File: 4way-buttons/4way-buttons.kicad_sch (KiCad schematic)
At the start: 8 parts, among them J1 Conn_01x08_Male, J2 Conn_01x08_Male, SW1 SW_Push, SW2 SW_Push, SW3 SW_Push, SW4 SW_Push, SW5 SW_Push, SW6 SW_Push

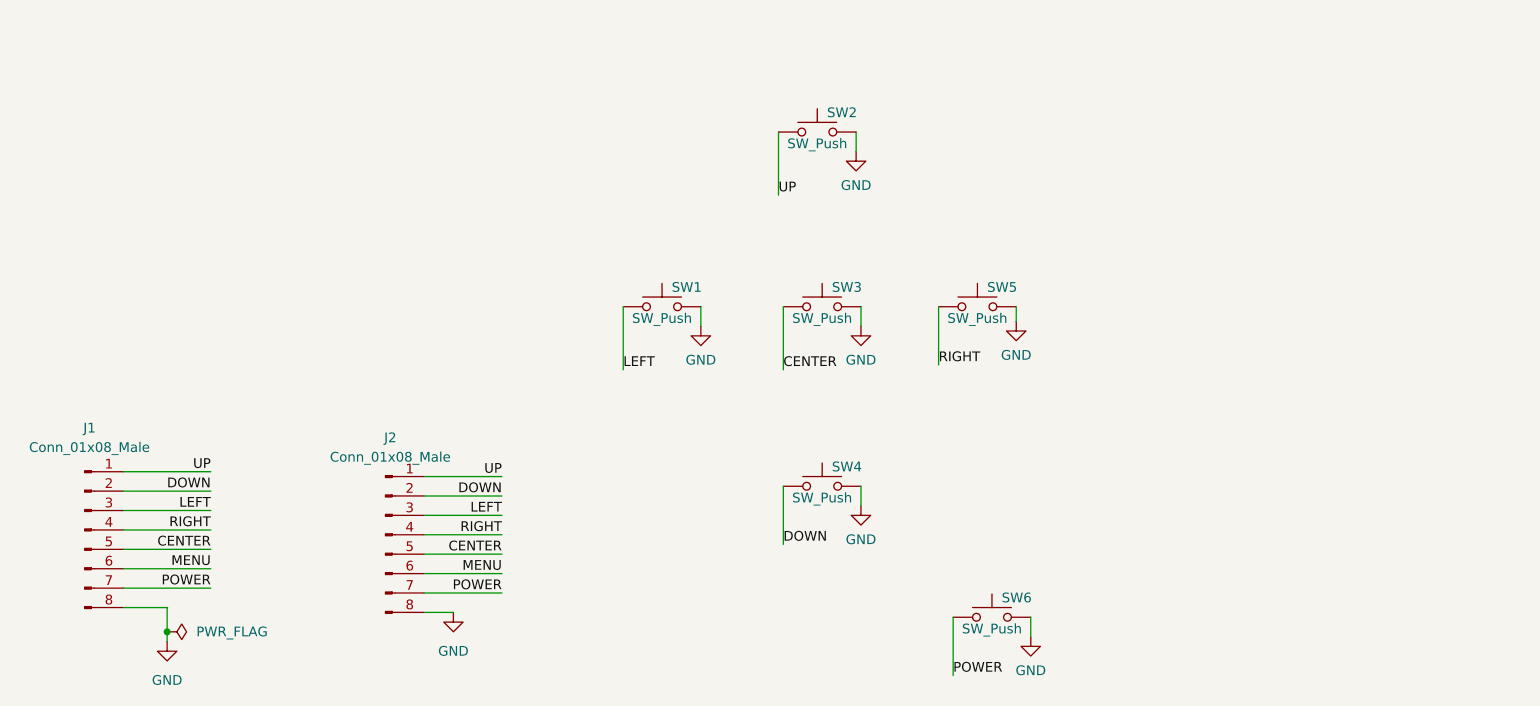
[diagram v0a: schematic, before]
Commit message: 모니터 컨트를 버튼 보드 이미지 추가
Signed-off-by: Ju, Gyeong-min <jcmh74@gmail.com>
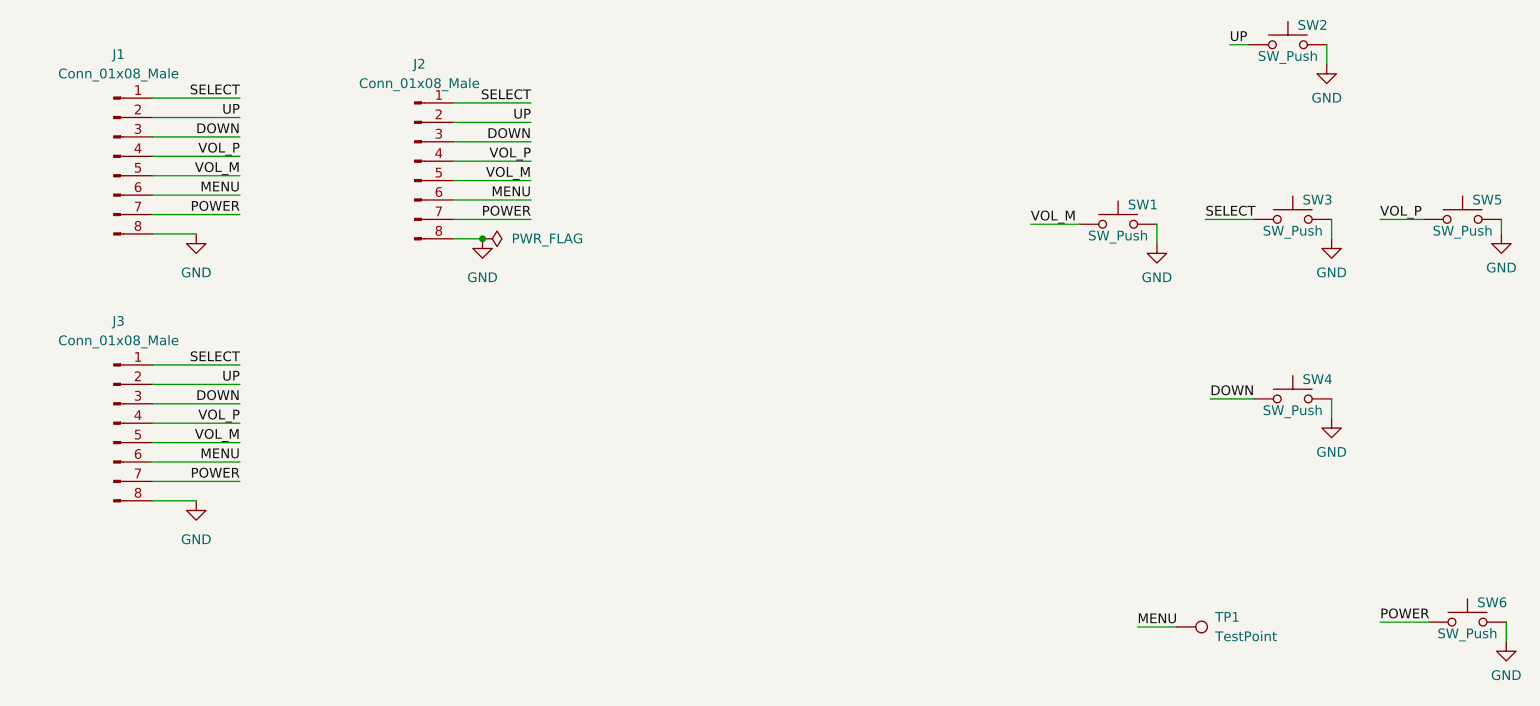
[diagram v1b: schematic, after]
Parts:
- added J3: Conn_01x08_Male, Connector_JST:JST_PH_S8B-PH-K_1x08_P2.00mm_Horizontal, symbol Connector:Conn_01x08_Male
- added TP1: TestPoint, TestPoint:TestPoint_Pad_D2.0mm, symbol Connector:TestPoint
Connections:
- net DOWN: now also J1.3 (Pin_3), J2.3 (Pin_3), J3.3 (Pin_3); no longer J1.2 (Pin_2), J2.2 (Pin_2)
- net GND: now also J3.8 (Pin_8)
- net MENU: now also J3.6 (Pin_6), TP1.1
- net POWER: now also J3.7 (Pin_7)
- net UP: now also J1.2 (Pin_2), J2.2 (Pin_2), J3.2 (Pin_2); no longer J1.1 (Pin_1), J2.1 (Pin_1)
- net CENTER renamed VOL_M
- net VOL_M: now also SW1.1, J3.5 (Pin_5); no longer SW3.1
- removed net LEFT: J1.3 (Pin_3), J2.3 (Pin_3), SW1.1
- net RIGHT renamed VOL_P
- net VOL_P: now also J3.4 (Pin_4)
- new net SELECT: J1.1 (Pin_1), J2.1 (Pin_1), J3.1 (Pin_1), SW3.1
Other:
- moved on the sheet: J1, J2, SW1, SW2, SW3, SW4, SW5, SW6
